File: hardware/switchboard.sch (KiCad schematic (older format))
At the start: 0 parts

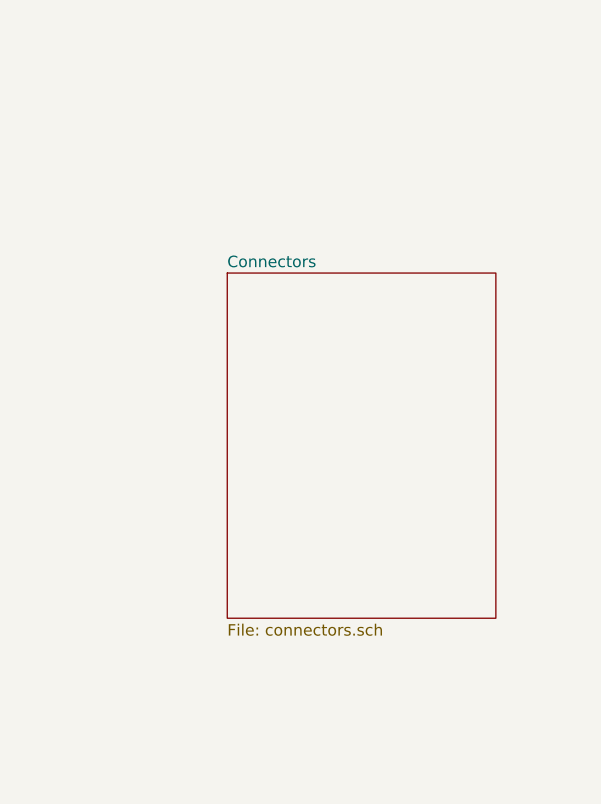
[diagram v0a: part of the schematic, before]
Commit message: hardware: export connectors connections
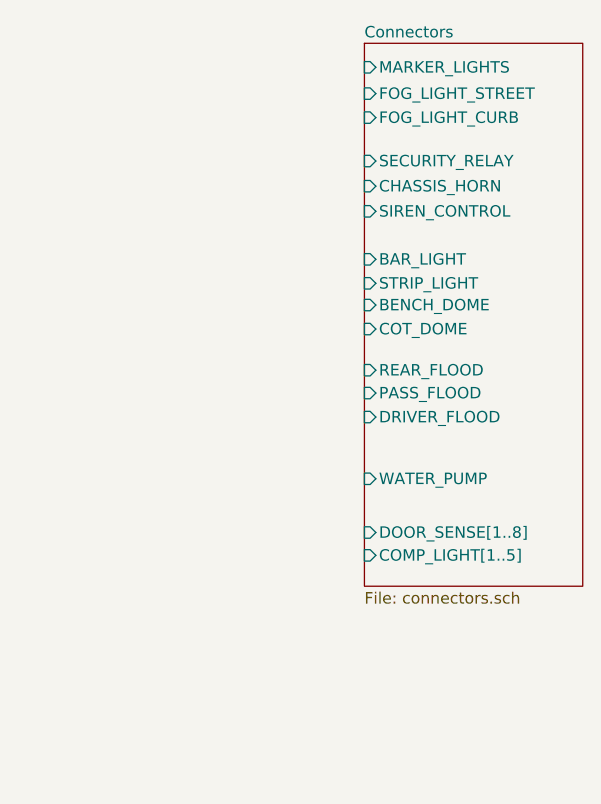
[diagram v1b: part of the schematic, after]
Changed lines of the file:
@@
-$EndSheet
-$Sheet
-S 8665 1875 1175 1510
-U 605C149A
-F0 "Connectors" 50
-F1 "connectors.sch" 50
 $EndSheet
 $Sheet
@@
 F1 "mcu.sch" 50
 $EndSheet
+$Sheet
+S 9265 870  955  2375
+U 605C149A
+F0 "Connectors" 50
+F1 "connectors.sch" 50
+F2 "MARKER_LIGHTS" I L 9265 975 50
+F3 "FOG_LIGHT_STREET" I L 9265 1090 50
+F4 "FOG_LIGHT_CURB" I L 9265 1195 50
+F5 "SECURITY_RELAY" I L 9265 1385 50
+F6 "CHASSIS_HORN" I L 9265 1495 50
+F7 "SIREN_CONTROL" I L 9265 1605 50
+F8 "BAR_LIGHT" I L 9265 1815 50
+F9 "WATER_PUMP" I L 9265 2775 50
+F10 "BENCH_DOME" I L 9265 2015 50
+F11 "COT_DOME" I L 9265 2120 50
+F12 "REAR_FLOOD" I L 9265 2300 50
+F13 "STRIP_LIGHT" I L 9265 1920 50
+F14 "PASS_FLOOD" I L 9265 2400 50
+F15 "DRIVER_FLOOD" I L 9265 2505 50
+F16 "DOOR_SENSE[1..8]" I L 9265 3010 50
+F17 "COMP_LIGHT[1..5]" I L 9265 3110 50
+$EndSheet
 $EndSCHEMATC

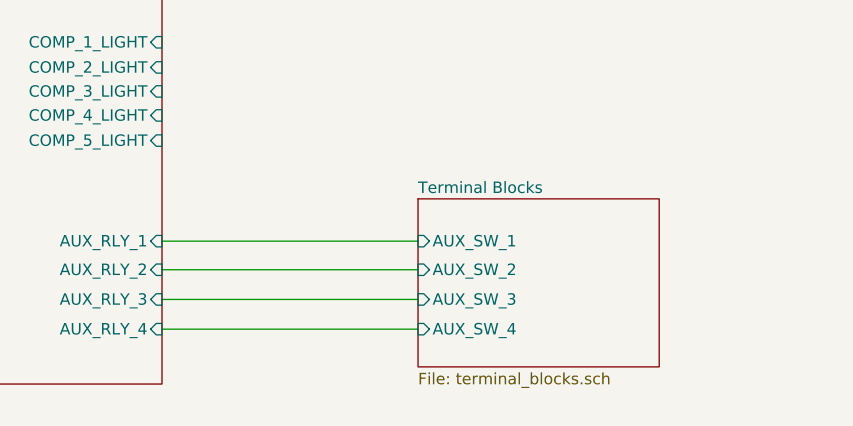
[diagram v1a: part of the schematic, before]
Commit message: hardware: remove terminal blocks
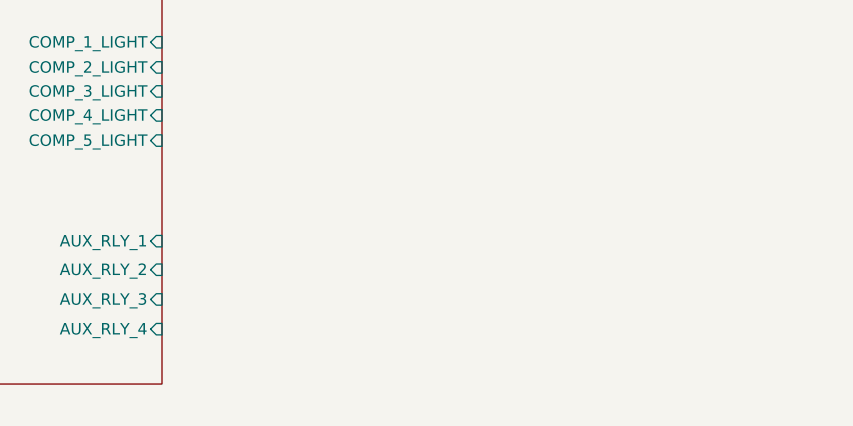
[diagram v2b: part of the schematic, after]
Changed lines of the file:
@@
 $Descr A4 11693 8268
 encoding utf-8
-Sheet 1 6
+Sheet 1 5
 Title ""
 Date ""
@@
 $EndSheet
 $Sheet
-S 7830 4840 1055 735
-U 60B2977E
-F0 "Terminal Blocks" 50
-F1 "terminal_blocks.sch" 50
-F2 "AUX_SW_1" I L 7830 5025 50
-F3 "AUX_SW_2" I L 7830 5150 50
-F4 "AUX_SW_3" I L 7830 5280 50
-F5 "AUX_SW_4" I L 7830 5410 50
-$EndSheet
-Wire Wire Line
-	6710 5025 7830 5025
-Wire Wire Line
-	6710 5150 7830 5150
-Wire Wire Line
-	6710 5280 7830 5280
-Wire Wire Line
-	6710 5410 7830 5410
-$Sheet
 S 2020 3100 1350 1410

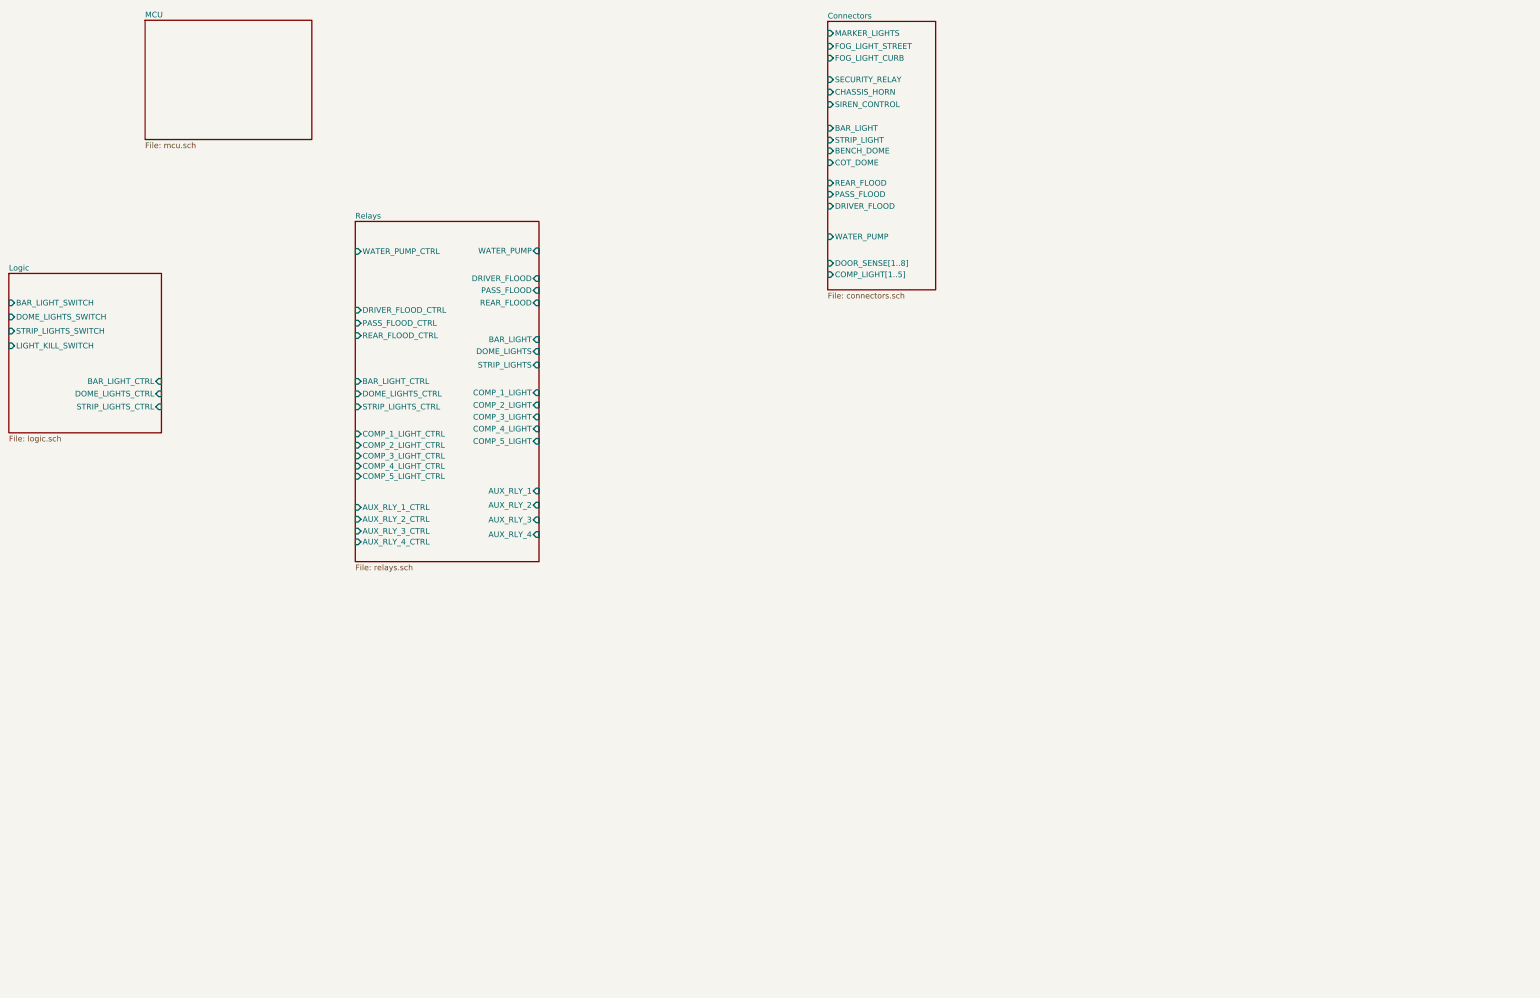
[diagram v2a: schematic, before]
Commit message: hardware: migrate hierarchical pins to busses
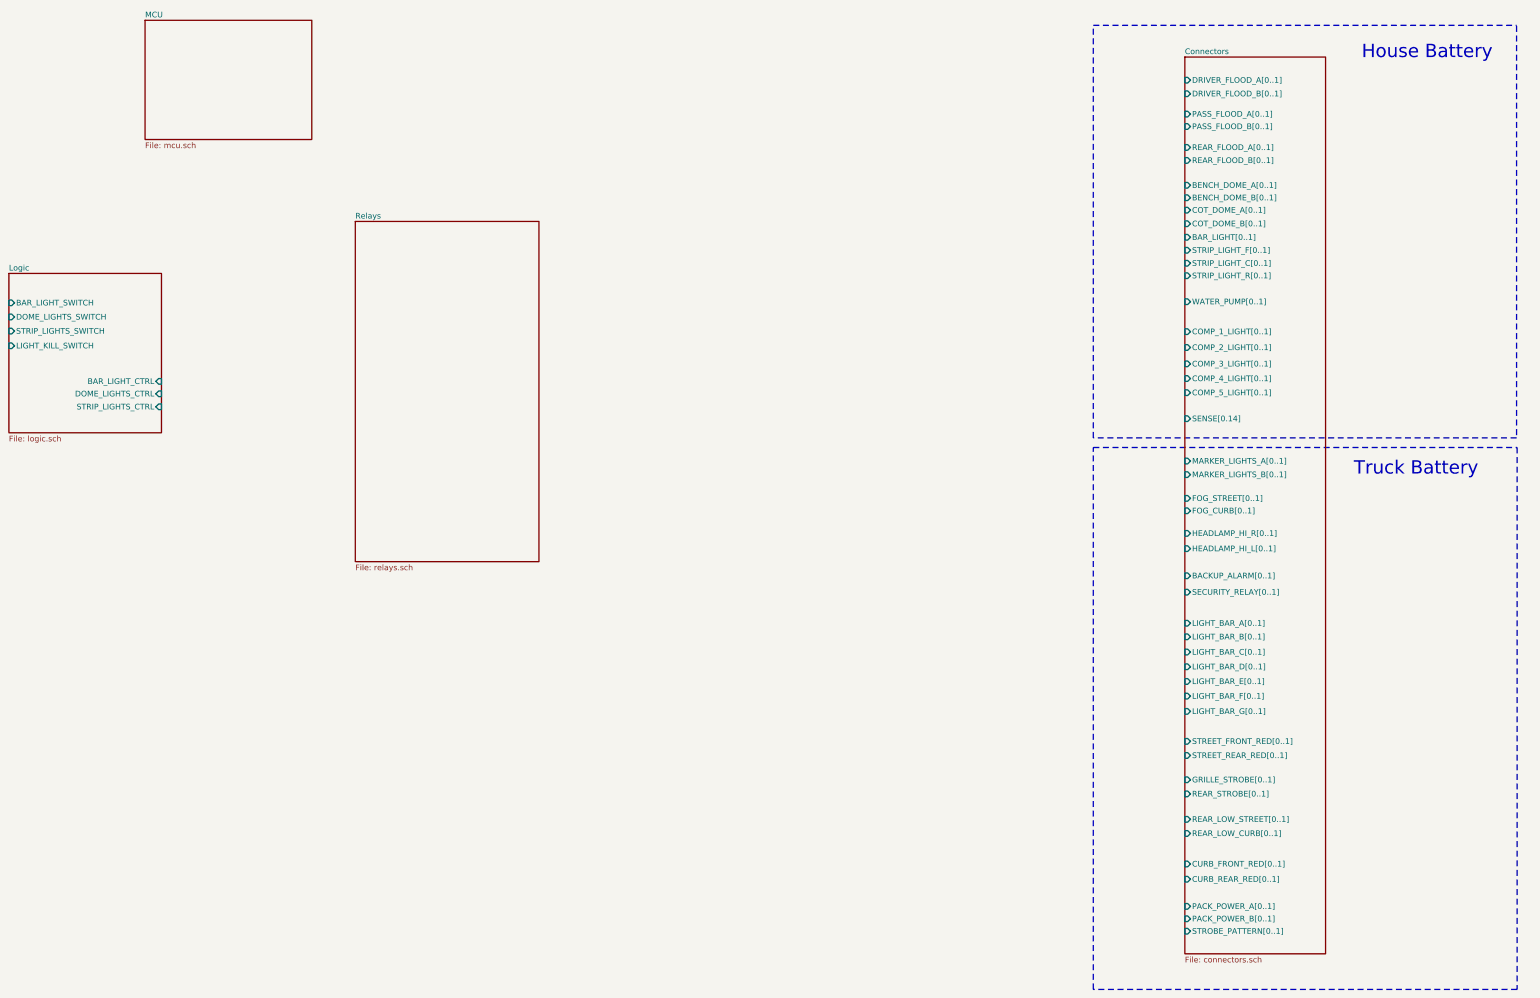
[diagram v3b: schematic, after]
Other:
- note added: "House Battery"
- note added: "Truck Battery"
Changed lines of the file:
@@
 EELAYER 30 0
 EELAYER END
-$Descr A4 11693 8268
+$Descr A3 16535 11693
 encoding utf-8
 Sheet 1 5
@@
 Comment4 ""
 $EndDescr
-$Sheet
-S 5085 2640 1625 3010
-U 605C1303
-F0 "Relays" 50
-F1 "relays.sch" 50
-F2 "DOME_LIGHTS" I R 6710 3790 50
-F3 "WATER_PUMP" I R 6710 2900 50
-F4 "STRIP_LIGHTS" I R 6710 3910 50
-F5 "REAR_FLOOD" I R 6710 3360 50
-F6 "DRIVER_FLOOD" I R 6710 3145 50
-F7 "PASS_FLOOD" I R 6710 3250 50
-F8 "DOME_LIGHTS_CTRL" I L 5085 4165 50
-F9 "WATER_PUMP_CTRL" I L 5085 2905 50
-F10 "STRIP_LIGHTS_CTRL" I L 5085 4280 50
-F11 "PASS_FLOOD_CTRL" I L 5085 3540 50
-F12 "DRIVER_FLOOD_CTRL" I L 5085 3425 50
-F13 "REAR_FLOOD_CTRL" I L 5085 3650 50
-F14 "BAR_LIGHT" I R 6710 3685 50
-F15 "BAR_LIGHT_CTRL" I L 5085 4055 50
-F16 "COMP_1_LIGHT_CTRL" I L 5085 4520 50
-F17 "COMP_1_LIGHT" I R 6710 4155 50
-F18 "COMP_4_LIGHT" I R 6710 4475 50
-F19 "COMP_4_LIGHT_CTRL" I L 5085 4805 50
-F20 "COMP_3_LIGHT" I R 6710 4370 50
-F21 "COMP_3_LIGHT_CTRL" I L 5085 4715 50
-F22 "COMP_2_LIGHT" I R 6710 4265 50
-F23 "COMP_2_LIGHT_CTRL" I L 5085 4620 50
-F24 "COMP_5_LIGHT_CTRL" I L 5085 4895 50
-F25 "COMP_5_LIGHT" I R 6710 4585 50
-F26 "AUX_RLY_1" I R 6710 5025 50
-F27 "AUX_RLY_1_CTRL" I L 5085 5170 50
-F28 "AUX_RLY_2" I R 6710 5150 50
-F29 "AUX_RLY_2_CTRL" I L 5085 5275 50
-F30 "AUX_RLY_3" I R 6710 5280 50
-F31 "AUX_RLY_3_CTRL" I L 5085 5380 50
-F32 "AUX_RLY_4" I R 6710 5410 50
-F33 "AUX_RLY_4_CTRL" I L 5085 5475 50
-$EndSheet
 $Sheet
 S 2020 3100 1350 1410
@@
 $EndSheet
 $Sheet
-S 9265 870  955  2375
+S 5085 2640 1625 3010
+U 605C1303
+F0 "Relays" 50
+F1 "relays.sch" 50
+$EndSheet
+$Sheet
+S 12425 1185 1245 7935
 U 605C149A
 F0 "Connectors" 50
 F1 "connectors.sch" 50
-F2 "MARKER_LIGHTS" I L 9265 975 50
-F3 "FOG_LIGHT_STREET" I L 9265 1090 50
-F4 "FOG_LIGHT_CURB" I L 9265 1195 50
-F5 "SECURITY_RELAY" I L 9265 1385 50
-F6 "CHASSIS_HORN" I L 9265 1495 50
-F7 "SIREN_CONTROL" I L 9265 1605 50
-F8 "BAR_LIGHT" I L 9265 1815 50
-F9 "WATER_PUMP" I L 9265 2775 50
-F10 "BENCH_DOME" I L 9265 2015 50
-F11 "COT_DOME" I L 9265 2120 50
-F12 "REAR_FLOOD" I L 9265 2300 50
-F13 "STRIP_LIGHT" I L 9265 1920 50
-F14 "PASS_FLOOD" I L 9265 2400 50
-F15 "DRIVER_FLOOD" I L 9265 2505 50
-F16 "DOOR_SENSE[1..8]" I L 9265 3010 50
-F17 "COMP_LIGHT[1..5]" I L 9265 3110 50
+F2 "DRIVER_FLOOD_A[0..1]" I L 12425 1390 50
+F3 "STROBE_PATTERN[0..1]" I L 12425 8920 50
+F4 "BACKUP_ALARM[0..1]" I L 12425 5775 50
+F5 "SECURITY_RELAY[0..1]" I L 12425 5920 50
+F6 "MARKER_LIGHTS_A[0..1]" I L 12425 4760 50
+F7 "FOG_CURB[0..1]" I L 12425 5200 50
+F8 "FOG_STREET[0..1]" I L 12425 5090 50
+F9 "PASS_FLOOD_A[0..1]" I L 12425 1690 50
+F10 "REAR_FLOOD_A[0..1]" I L 12425 1985 50
+F11 "BENCH_DOME_A[0..1]" I L 12425 2320 50
+F12 "COT_DOME_A[0..1]" I L 12425 2540 50
+F13 "STRIP_LIGHT_C[0..1]" I L 12425 3010 50
+F14 "WATER_PUMP[0..1]" I L 12425 3350 50
+F15 "BAR_LIGHT[0..1]" I L 12425 2780 50
+F16 "HEADLAMP_HI_R[0..1]" I L 12425 5400 50
+F17 "HEADLAMP_HI_L[0..1]" I L 12425 5535 50
+F18 "STRIP_LIGHT_F[0..1]" I L 12425 2895 50
+F19 "COMP_5_LIGHT[0..1]" I L 12425 4155 50
+F20 "COMP_4_LIGHT[0..1]" I L 12425 4030 50
+F21 "COMP_3_LIGHT[0..1]" I L 12425 3900 50
+F22 "COMP_2_LIGHT[0..1]" I L 12425 3755 50
+F23 "COMP_1_LIGHT[0..1]" I L 12425 3615 50
+F24 "SENSE[0.14]" I L 12425 4385 50
+F25 "LIGHT_BAR_F[0..1]" I L 12425 6840 50
+F26 "LIGHT_BAR_E[0..1]" I L 12425 6710 50
+F27 "LIGHT_BAR_D[0..1]" I L 12425 6580 50
+F28 "LIGHT_BAR_C[0..1]" I L 12425 6450 50
+F29 "LIGHT_BAR_B[0..1]" I L 12425 6315 50
+F30 "STREET_REAR_RED[0..1]" I L 12425 7365 50
+F31 "STREET_FRONT_RED[0..1]" I L 12425 7240 50
+F32 "GRILLE_STROBE[0..1]" I L 12425 7580 50
+F33 "REAR_STROBE[0..1]" I L 12425 7705 50
+F34 "REAR_LOW_CURB[0..1]" I L 12425 8055 50
+F35 "REAR_LOW_STREET[0..1]" I L 12425 7930 50
+F36 "PACK_POWER_A[0..1]" I L 12425 8700 50
+F37 "PACK_POWER_B[0..1]" I L 12425 8810 50
+F38 "CURB_REAR_RED[0..1]" I L 12425 8460 50
+F39 "CURB_FRONT_RED[0..1]" I L 12425 8325 50
+F40 "LIGHT_BAR_G[0..1]" I L 12425 6975 50
+F41 "LIGHT_BAR_A[0..1]" I L 12425 6195 50
+F42 "MARKER_LIGHTS_B[0..1]" I L 12425 4880 50
+F43 "DRIVER_FLOOD_B[0..1]" I L 12425 1510 50
+F44 "PASS_FLOOD_B[0..1]" I L 12425 1800 50
+F45 "REAR_FLOOD_B[0..1]" I L 12425 2100 50
+F46 "BENCH_DOME_B[0..1]" I L 12425 2430 50
+F47 "COT_DOME_B[0..1]" I L 12425 2660 50
+F48 "STRIP_LIGHT_R[0..1]" I L 12425 3120 50
 $EndSheet
+Wire Notes Line
+	15360 4555 11615 4555
+Wire Notes Line
+	11615 4555 11615 905
+Wire Notes Line
+	11615 905  15360 905
+Wire Notes Line
+	15360 910  15360 4560
+Text Notes 13990 1210 0    118  ~ 0
+House Battery
+Wire Notes Line
+	11615 4640 15365 4640
+Wire Notes Line
+	15365 4640 15365 9435
+Wire Notes Line
+	15365 9435 11615 9435
+Wire Notes Line
+	11615 9435 11615 4640
+Text Notes 13920 4895 0    118  ~ 0
+Truck Battery
 $EndSCHEMATC

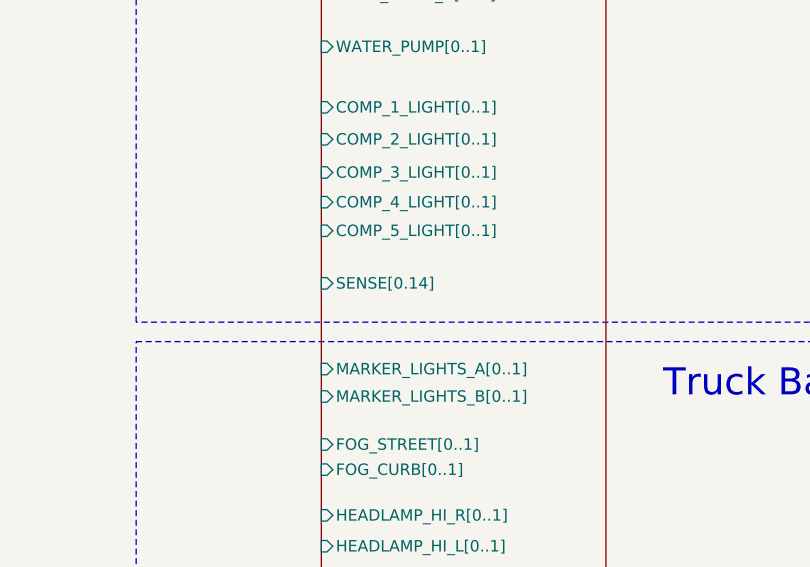
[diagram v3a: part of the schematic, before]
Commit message: hardware: fix mislabeled bus
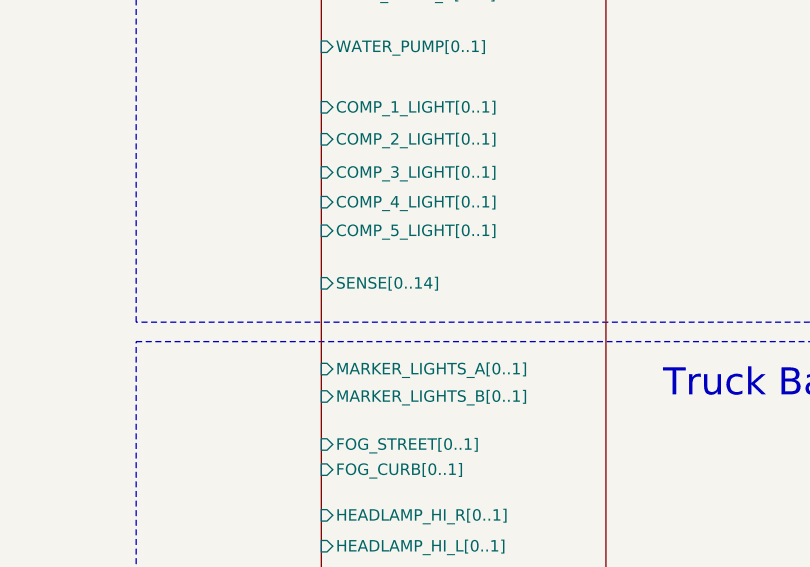
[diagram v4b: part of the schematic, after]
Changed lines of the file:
@@
 F22 "COMP_2_LIGHT[0..1]" I L 12425 3755 50
 F23 "COMP_1_LIGHT[0..1]" I L 12425 3615 50
-F24 "SENSE[0.14]" I L 12425 4385 50
+F24 "SENSE[0..14]" I L 12425 4385 50
 F25 "LIGHT_BAR_F[0..1]" I L 12425 6840 50
 F26 "LIGHT_BAR_E[0..1]" I L 12425 6710 50
